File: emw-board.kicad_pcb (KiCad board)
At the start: 2 copper layers, 49.5 x 48.3 mm, 36 parts, among them P1 1WIRE, P2 BATT, P3 CONN_01X06, P4 SWDN, P5 CONS, P6 OLED, P7 CONN_01X07, SW1 B3S-1000, SW2 B3S-1000, U1 MAX604CSA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

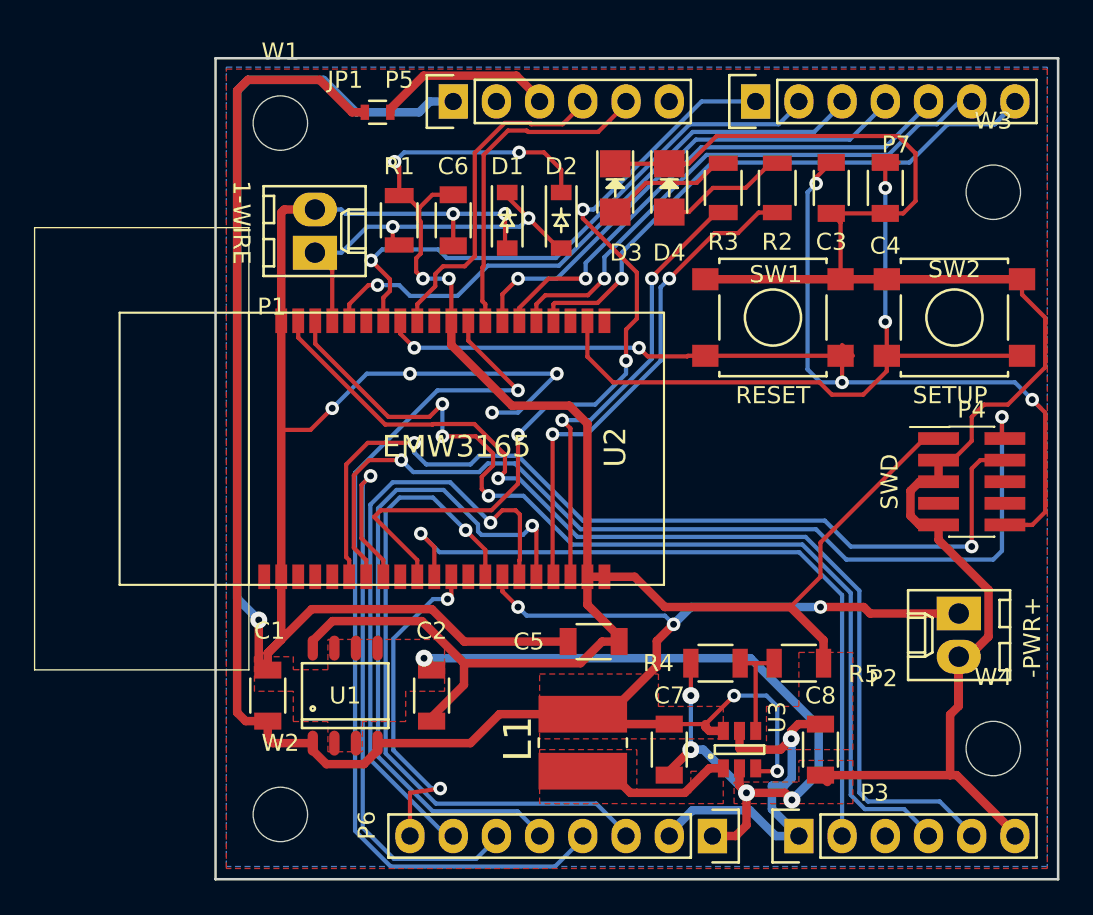
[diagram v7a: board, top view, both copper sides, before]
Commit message: Add solder jumpers for selecting power from ftdi console and batter level measurement enable/disable.
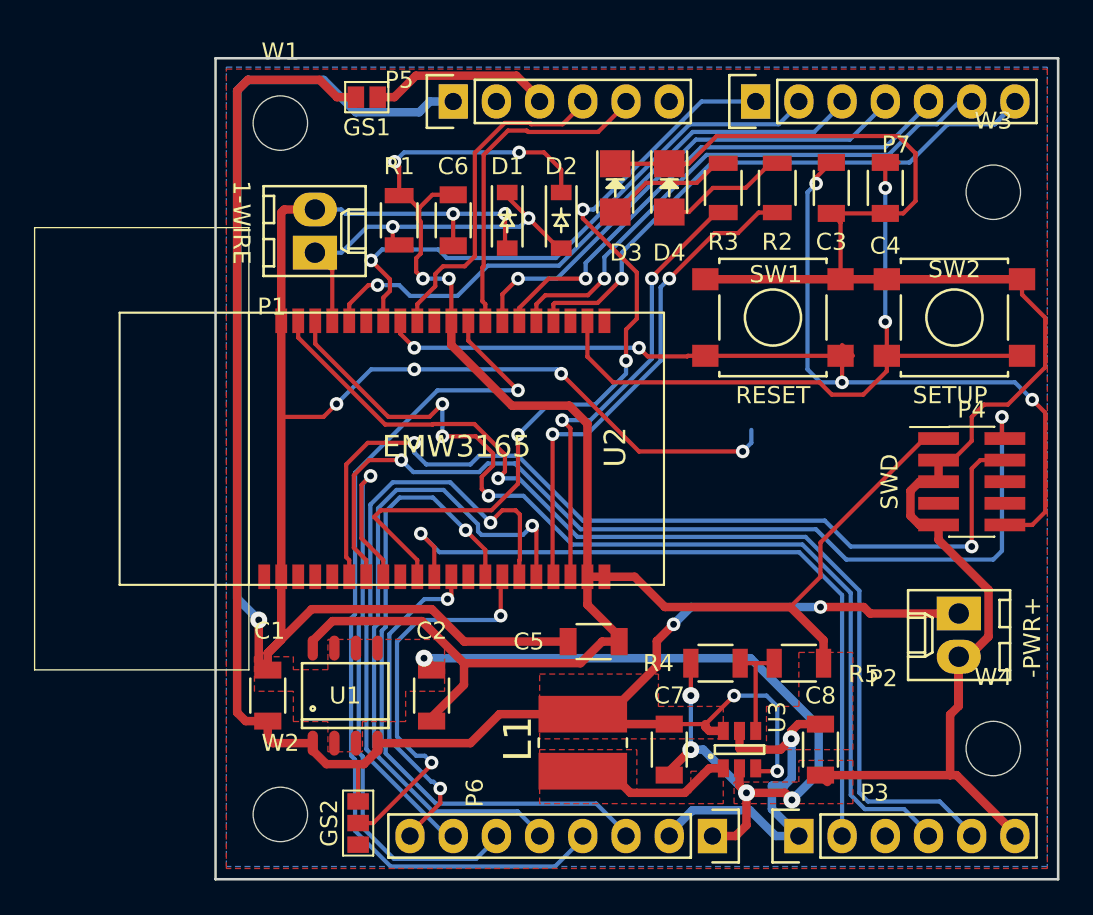
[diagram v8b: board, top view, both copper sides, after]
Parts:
- removed JP1: Jumper_NO_Small, Resistors_SMD:R_0603
- added GS1: GS2, GS2, F.Cu at (123.2, 55.6)
- added GS2: GS3, GS3, F.Cu at (122.7, 98.3)
- R2, R3: value 2K -> 270
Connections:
- U2 pad 34: +BATT -> Net-(GS2-Pad2)
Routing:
- net Net-(GS2-Pad2): track 0.00 -> 23.2 mm, vias 0 -> 2
- net +BATT: track 125.9 -> 115.5 mm, vias 5 -> 4
- net GND: track 292.0 -> 301.5 mm
- net Net-(C3-Pad1): track 68.1 -> 66.0 mm
- net OLED_CS: track 20.9 -> 20.4 mm
